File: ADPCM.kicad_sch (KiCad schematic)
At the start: 19 parts, among them IC111 M5205, IC114 TL072

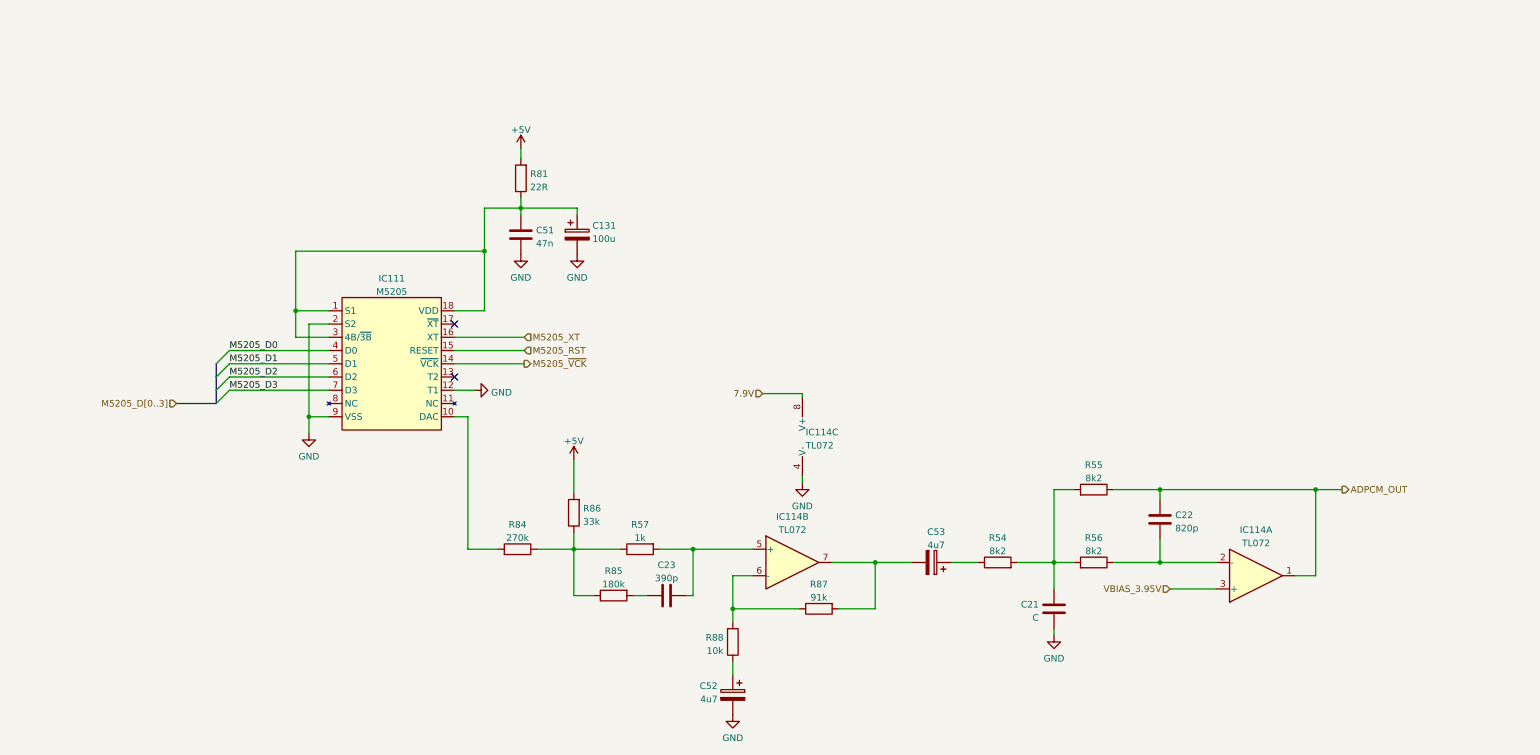
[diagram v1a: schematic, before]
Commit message: Fixed mistake in ADPCM page and added notes about opamps.
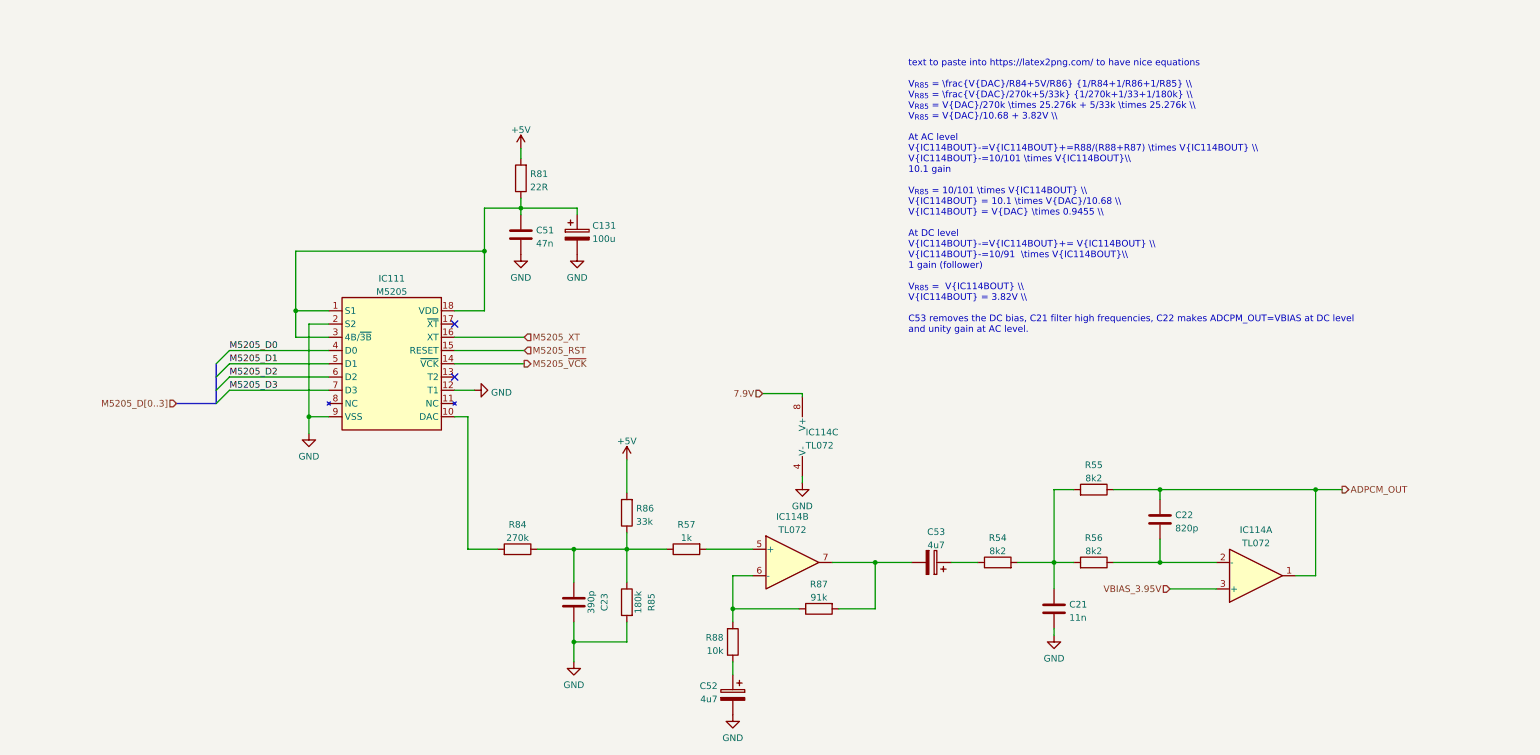
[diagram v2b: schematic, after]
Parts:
- C21: value C -> 11n
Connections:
- net GND: now also C23.2, R85.2
- net at C23.1: now also R57.1, R84.1, R85.1, R86.1; no longer R85.2
- net at IC114.5 (+), R57.2: no longer C23.2
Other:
- note added: "text to paste into https://latex2png.com/ to have nice equations V_{R85} = \frac{V{DAC}/R84+5V/R86} {1/R84+1/R86+1/R85} \\ V_{R85} = \frac{V{DAC}/270k+5/33k} {1/270k+1/33+1/180k} \\ V_{R85} = V{DAC}/270k \times 25.276k + 5/33k \times 25.276k \\ V_{R85} = V{DAC}/10.68 + 3.82V \\ At AC level V{IC114BOUT}-=V{IC114BOUT}+=R88/(R88+R87) \times V{IC114BOUT} \\ V{IC114BOUT}-=10/101 \times V{IC114BOUT}\\ 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"
- moved on the sheet: C23, R57, R85, R86

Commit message: All calculations added.
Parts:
- removed unit 3 of IC114
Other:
- note added: "text to paste into https://latex2png.com/ to have nice equations V_{R85} = \frac{V_{DAC}/R84+5V/R86} {1/R84+1/R86+1/R85} \\ V_{R85} = \frac{V_{DAC}/270k+5/33k} {1/270k+1/33+1/180k} \\ V_{R85} = V_{DAC}/270k \times 25.276k + 5/33k \times 25.276k \\ V_{R85} = V_{DAC}/10.68 + 3.82V \\ At AC level V_{IC114BOUT}- = V_{IC114BOUT}+ = R88/(R88+R87) \times V_{IC114BOUT} \\ V_{IC114BOUT}- = 10/101 \times V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"
- note removed: "text to paste into https://latex2png.com/ to have nice equations V_{R85} = \frac{V{DAC}/R84+5V/R86} {1/R84+1/R86+1/R85} \\ V_{R85} = \frac{V{DAC}/270k+5/33k} {1/270k+1/33+1/180k} \\ V_{R85} = V{DAC}/270k \times 25.276k + 5/33k \times 25.276k \\ V_{R85} = V{DAC}/10.68 + 3.82V \\ At AC level V{IC114BOUT}-=V{IC114BOUT}+=R88/(R88+R87) \times V{IC114BOUT} \\ V{IC114BOUT}-=10/101 \times V{IC114BOUT}\\ 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"

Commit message: Documentation started.
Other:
- note added: "text to paste into https://latex2png.com/ to have nice equations V_{R85} = \frac{V_{DAC}/R84+5V/R86} {1/R84+1/R86+1/R85} \\ V_{R85} = \frac{V_{DAC}/270k+5/33k} {1/270k+1/33+1/180k} \\ V_{R85} = V_{DAC}/270k \times 25.276k + 5/33k \times 25.276k \\ V_{R85} = V_{DAC}/10.68 + 3.82V \\ At AC level V_{IC114B-} = V_{IC114B+} = R88/(R88+R87) \times V_{IC114BOUT} \\ V_{IC114B-} = 10/101 \times V_{IC114BO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"
- note removed: "text to paste into https://latex2png.com/ to have nice equations V_{R85} = \frac{V_{DAC}/R84+5V/R86} {1/R84+1/R86+1/R85} \\ V_{R85} = \frac{V_{DAC}/270k+5/33k} {1/270k+1/33+1/180k} \\ V_{R85} = V_{DAC}/270k \times 25.276k + 5/33k \times 25.276k \\ V_{R85} = V_{DAC}/10.68 + 3.82V \\ At AC level V_{IC114BOUT}- = V_{IC114BOUT}+ = R88/(R88+R87) \times V_{IC114BOUT} \\ V_{IC114BOUT}- = 10/101 \times V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"
- title: (none) -> NEC PC-Engine IFU-30
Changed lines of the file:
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@@
 (kicad_sch (version 20211123) (generator eeschema)
   (paper "A4")
+  (title_block
+    (title "NEC PC-Engine IFU-30")
+    (date "2022-10-27")
+    (rev "0.1")
+    (comment 1 "Author: Regis Galland")
+    (comment 2 "NEC IFU-30 PCB reverse engineered schematics")
+  )
   (junction (at 128.27 127.635) (diameter 0) (color 0 0 0 0)
   )
@@
     (stroke (width 0) (type default) (color 0 0 0 0))
   )
-  (text "text to paste into https://latex2png.com/ to have nice equations\n\nV_{R85} = \\frac{V_{DAC}/R84+5V/R86} {1/R84+1/R86+1/R85} \\\\\nV_{R85} = \\frac{V_{DAC}/270k+5/33k} {1/270k+1/33+1/180k} \\\\\nV_{R85} = V_{DAC}/270k \\times 25.276k + 5/33k \\times 25.276k \\\\\nV_{R85} = V_{DAC}/10.68 + 3.82V \\\\\n\nAt AC level\nV_{IC114BOUT}- = V_{IC114BOUT}+ = R88/(R88+R87) \\times V_{IC114BOUT} \\\\\nV_{IC114BOUT}- = 10/101 \\times V_{IC114BOUT}\\\\\n10.1 gain\n\nV_{R85} = 10/101 \\times V_{IC114BOUT} \\\\\nV_{IC114BOUT} = 10.1 \\times V_{DAC}/10.68 \\\\\nV_{IC114BOUT} = V_{DAC} \\times 0.9455 \\\\\n\nAt DC level\nV_{R85} = V_{IC114BOUT}- = V_{IC114BOUT}+ = V_{IC114BOUT} \\\\\nV_{IC114BOUT} = 3.82V \\\\\n1 gain (follower)\n\nC53 removes the DC bias, C21 filter high frequencies, C22 makes ADCPM_OUT=VBIAS at DC level\nand unity gain at AC level.\n"
-    (at 182.245 86.36 0)
+  (text "text to paste into https://latex2png.com/ to have nice equations\n\nV_{R85} = \\frac{V_{DAC}/R84+5V/R86} {1/R84+1/R86+1/R85} \\\\\nV_{R85} = \\frac{V_{DAC}/270k+5/33k} {1/270k+1/33+1/180k} \\\\\nV_{R85} = V_{DAC}/270k \\times 25.276k + 5/33k \\times 25.276k \\\\\nV_{R85} = V_{DAC}/10.68 + 3.82V \\\\\n\nAt AC level\nV_{IC114B-} = V_{IC114B+} = R88/(R88+R87) \\times V_{IC114BOUT} \\\\\nV_{IC114B-} = 10/101 \\times V_{IC114BOUT}\\\\\nV_{IC114BOUT} = 101/10 \\times V_{IC114B-}\\\\\n\n101/10 = 10.1 gain\n\nV_{R85} = 10/101 \\times V_{IC114BOUT} \\\\\nV_{IC114BOUT} = 10.1 \\times V_{DAC}/10.68 \\\\\nV_{IC114BOUT} = V_{DAC} \\times 0.9455 \\\\\n\nAt DC level\nV_{R85} = V_{IC114B-} = V_{IC114B+} = V_{IC114BOUT} \\\\\nV_{IC114BOUT} = 3.82V \\\\\nunity gain (follower)\n\nC53 removes the DC bias introduced by IC114B, C21 filters high frequencies, C22 makes ADCPM_OUT=VBIAS at DC level\nand unity gain at AC level.\n"
+    (at 161.925 90.17 0)
     (effects (font (size 1.27 1.27)) (justify left bottom))
   )

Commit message: Documentation update
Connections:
- net at R57.1, R84.1, R85.1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: no longer C23.1
- net at IC114.5 (+), R57.2: now also C23.1
- net VBIAS_3.95V renamed VBIAS_3.9V
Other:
- note removed: "text to paste into https://latex2png.com/ to have nice equations V_{R85} = \frac{V_{DAC}/R84+5V/R86} {1/R84+1/R86+1/R85} \\ V_{R85} = \frac{V_{DAC}/270k+5/33k} {1/270k+1/33+1/180k} \\ V_{R85} = V_{DAC}/270k \times 25.276k + 5/33k \times 25.276k \\ V_{R85} = V_{DAC}/10.68 + 3.82V \\ At AC level V_{IC114B-} = V_{IC114B+} = R88/(R88+R87) \times V_{IC114BOUT} \\ V_{IC114B-} = 10/101 \times V_{IC114BO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"
- moved on the sheet: C131, C21, C22, C23, C51, C52, C53, IC111, IC114A, IC114B, R54, R55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

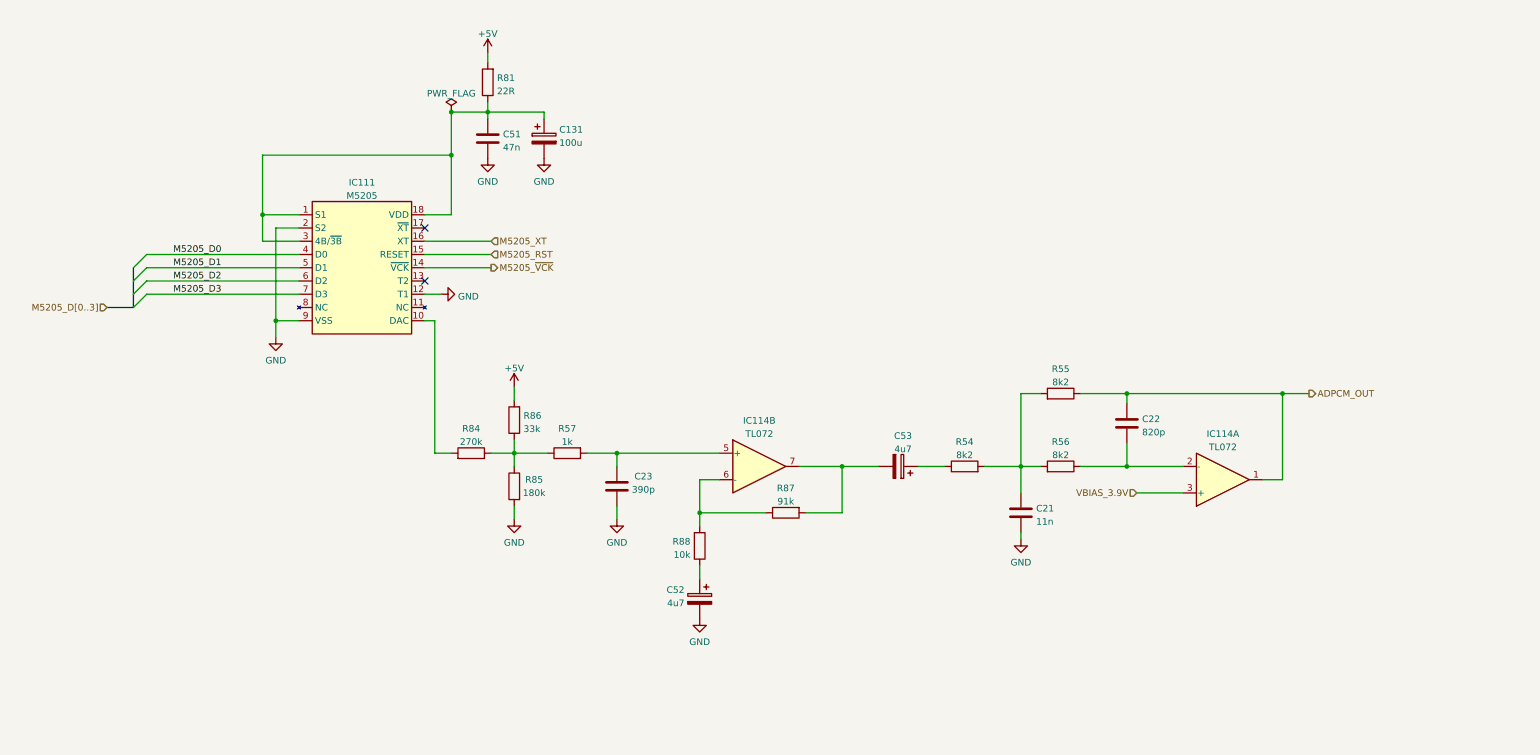
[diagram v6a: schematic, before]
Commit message: Fixed a few typos and mainly renamed connections to CD-ROM with more accurate descriptions
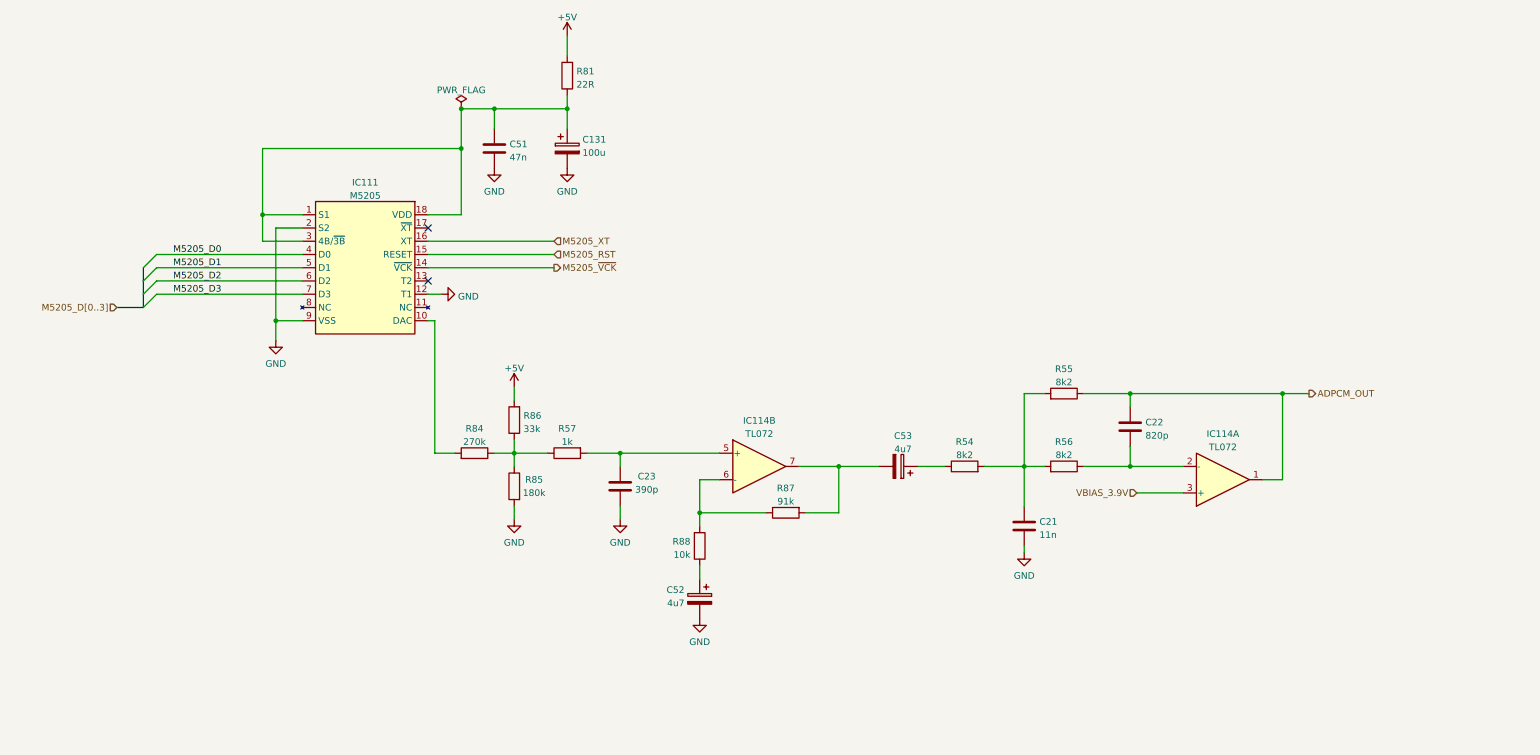
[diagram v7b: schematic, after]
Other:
- moved on the sheet: C131, C21, C22, C23, C51, IC111, R55, R56, R81, R84
